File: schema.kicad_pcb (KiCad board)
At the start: 2 copper layers, 59.7 x 41.3 mm, 4 parts, among them U1 74HC595D, U2 74HC595D, U5 28C256

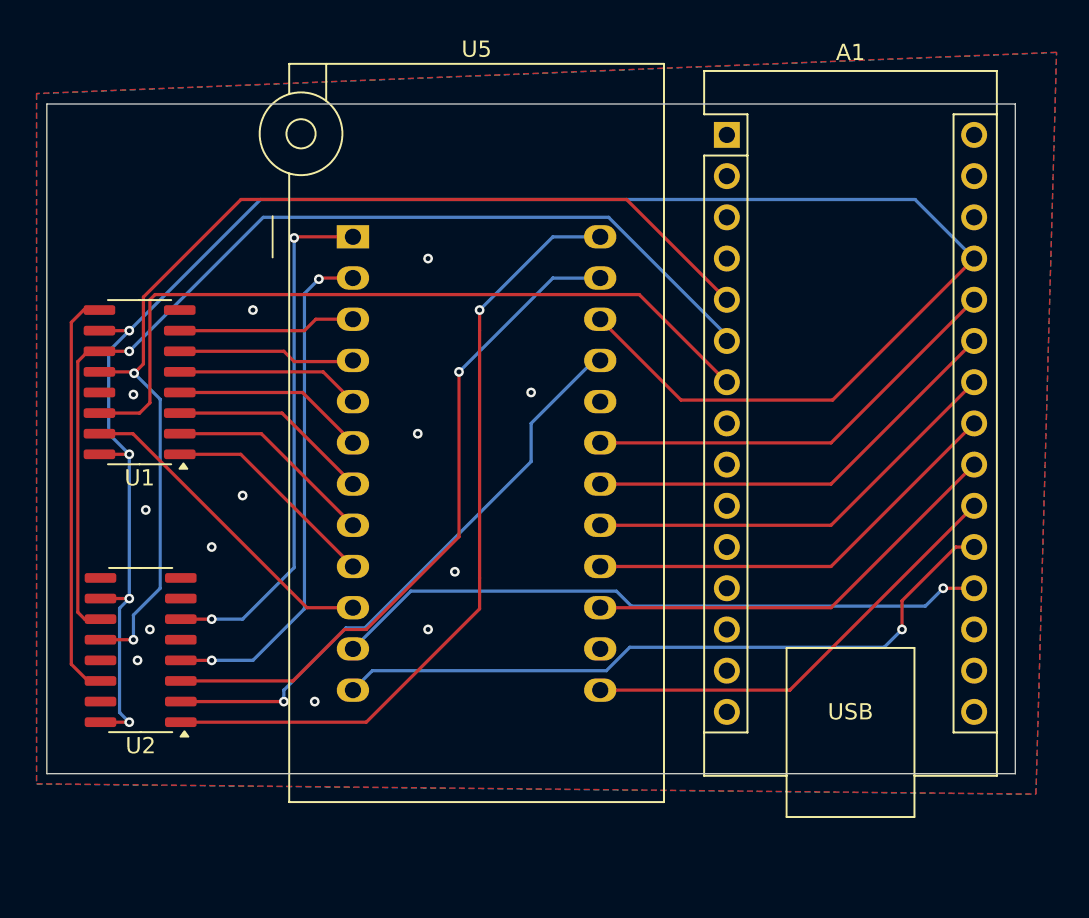
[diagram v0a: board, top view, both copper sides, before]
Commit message: fix-wrong-zif
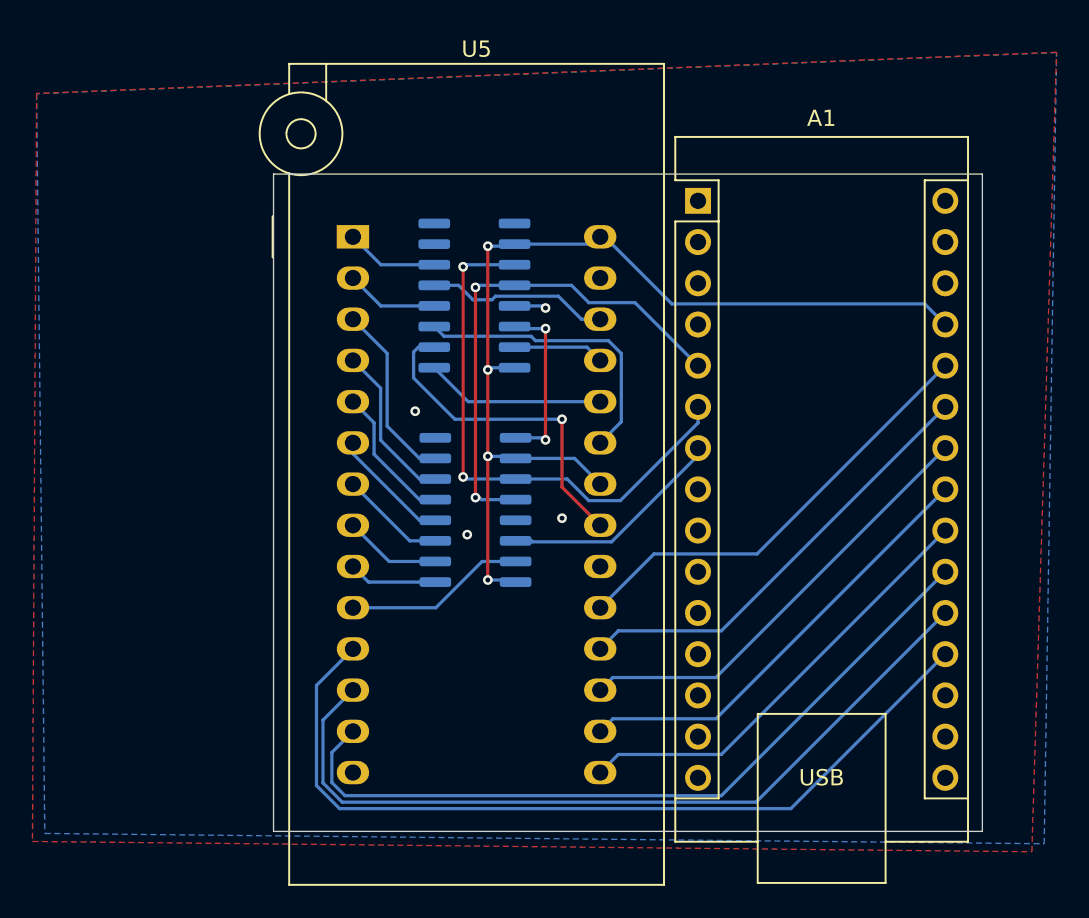
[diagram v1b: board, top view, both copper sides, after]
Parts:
- U1, U2: moved to B.Cu
- U5: value 28C256 -> AT28C256-15PU; footprint Socket:DIP_Socket-24_W11.9_W12.7_W15.24_W17.78_W18.5_3M_224-1275-00-0602J -> Socket:DIP_Socket-28_W11.9_W12.7_W15.24_W17.78_W18.5_3M_228-1277-00-0602J
- moved U2 30.0 mm to (133.0, 88.6), turned to 0 degrees
- moved U1 22.1 mm to (133.1, 101.9), turned to 0 degrees
- moved A1 4.44 mm to (146.8, 82.8)
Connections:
- A1 pad 27: /+5V -> +5VD
- U1 pad 10: /+5V -> +5VD
- U1 pad 16: /+5V -> +5VD
- U2 pad 10: /+5V -> +5VD
- U2 pad 16: /+5V -> +5VD
- U5 pad 22: /+5V -> +5VD
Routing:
- net /+5V: track 118.6 -> 0.00 mm, vias 4 -> 0
- net +5VD: track 0.00 -> 62.3 mm, vias 0 -> 4
- net Net-(U2-QB): track 49.0 -> 11.1 mm, vias 1 -> 0
- net Net-(A1-D2): track 67.9 -> 31.2 mm
- net Net-(A1-D4): track 47.7 -> 13.9 mm
- net Net-(A1-D3): track 64.1 -> 34.2 mm, vias 1 -> 2
- net Net-(U2-QG): track 32.3 -> 5.72 mm, vias 2 -> 0
- net Net-(U2-QE): track 31.8 -> 5.72 mm, vias 2 -> 0
- net Net-(U2-QD): track 42.1 -> 18.3 mm, vias 1 -> 0
- net Net-(A1-A2): track 27.8 -> 47.6 mm
- net Net-(U2-QC): track 36.4 -> 20.7 mm
- net Net-(U1-QH'): track 25.3 -> 10.7 mm, vias 0 -> 2
- net Net-(A1-A0): track 40.6 -> 52.6 mm, vias 1 -> 0
- net Net-(U2-QF): track 0.00 -> 11.3 mm
- net Net-(U1-QA): track 20.1 -> 11.2 mm
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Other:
- board size 59.7 x 41.3 mm -> 43.7 x 40.5 mm
- board text added: "Erinnerlichkeit V0.0.3 Proliecan"

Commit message: small corrections
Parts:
- added C1: 100nC, Capacitor_SMD:C_0805_2012Metric_Pad1.18x1.45mm_HandSolder, B.Cu at (143.3, 82.8)
- added C2: 100nC, Capacitor_SMD:C_0805_2012Metric_Pad1.18x1.45mm_HandSolder, B.Cu at (158.2, 90.7)
- added C3: 100nC, Capacitor_SMD:C_0805_2012Metric_Pad1.18x1.45mm_HandSolder, B.Cu at (132.8, 111.5)
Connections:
- net Net-(A1-A0) renamed /D0
- net Net-(A1-A1) renamed /D1
- net Net-(A1-A2) renamed /D2
- net Net-(A1-A3) renamed /D3
- net Net-(A1-A6) renamed /D6
- net Net-(A1-A7) renamed /D7
- net Net-(A1-SCL/A5) renamed /D5
- net Net-(A1-SDA/A4) renamed /D4
- net Net-(U1-QA) renamed /A0
- net Net-(U1-QB) renamed /A1
- net Net-(U1-QC) renamed /A2
- net Net-(U1-QD) renamed /A3
- net Net-(U1-QE) renamed /A4
- net Net-(U1-QF) renamed /A5
- net Net-(U1-QG) renamed /A6
- net Net-(U1-QH) renamed /A7
- net Net-(U2-QA) renamed /A8
- net Net-(U2-QB) renamed /A9
- net Net-(U2-QC) renamed /A10
- net Net-(U2-QD) renamed /A11
- net Net-(U2-QE) renamed /A12
- net Net-(U2-QF) renamed /A13
- net Net-(U2-QG) renamed /A14
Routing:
- net +5VD: track 62.3 -> 77.0 mm

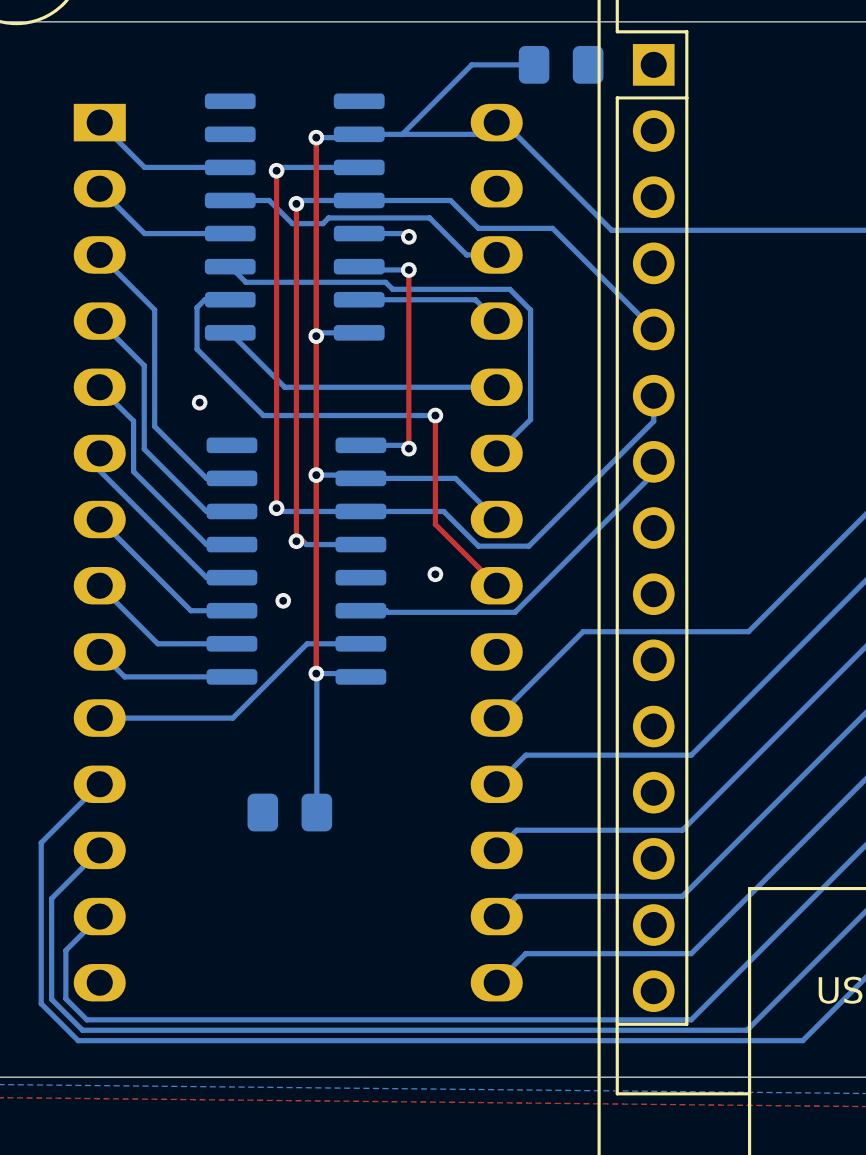
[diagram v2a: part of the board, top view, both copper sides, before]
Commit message: Route traces (with warnings)
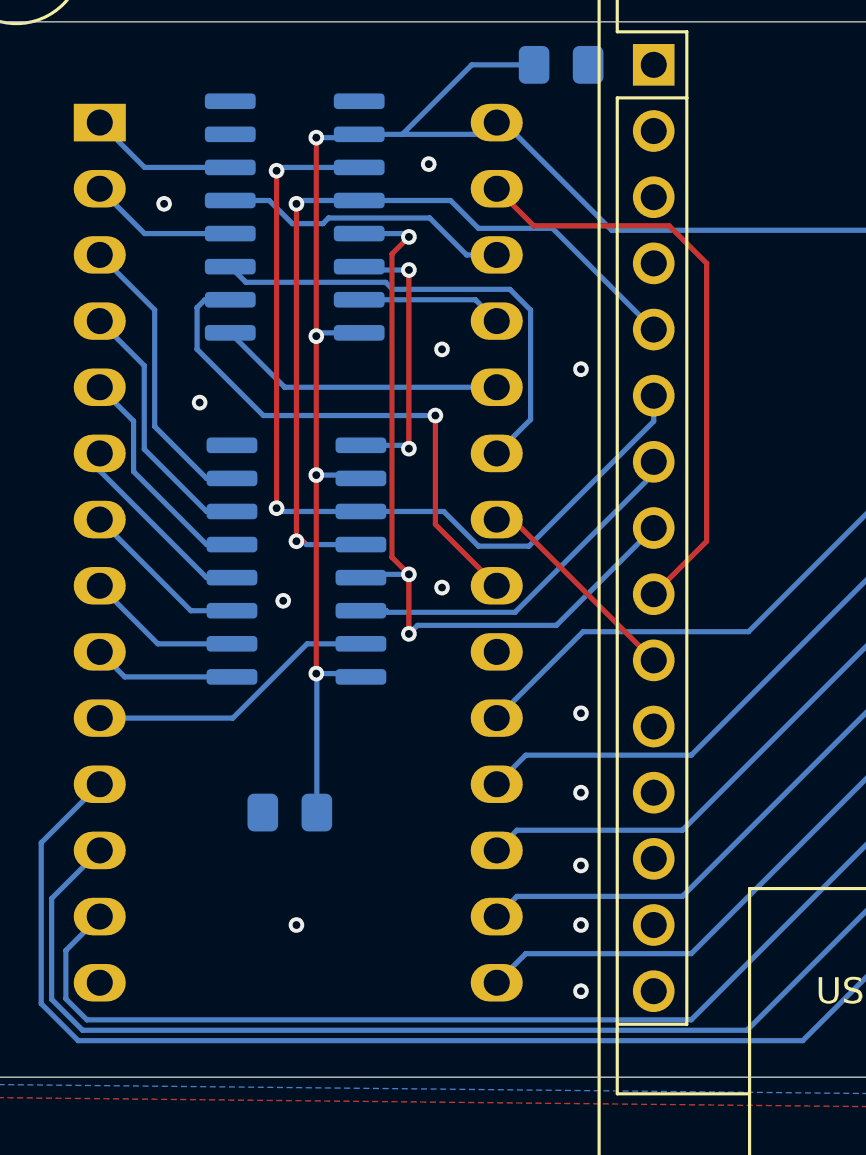
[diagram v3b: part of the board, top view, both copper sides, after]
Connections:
- A1 pad 10: unconnected-(A1-D7-Pad10) -> Net-(A1-D7)
- A1 pad 8: unconnected-(A1-D5-Pad8) -> Net-(A1-D5)
- A1 pad 9: unconnected-(A1-D6-Pad9) -> Net-(A1-D6)
- U1 pad 13: GNDD -> Net-(A1-D5)
- U2 pad 13: GNDD -> Net-(A1-D5)
- U5 pad 22: +5VD -> Net-(A1-D7)
- U5 pad 27: GNDD -> Net-(A1-D6)
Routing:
- net Net-(A1-D5): track 0.00 -> 30.7 mm, vias 0 -> 3
- net Net-(A1-D6): track 0.00 -> 22.8 mm
- net Net-(A1-D7): track 0.00 -> 8.27 mm
- net +5VD: track 77.0 -> 71.1 mm
- net GNDD: track 1.96 -> 0.00 mm, vias 4 -> 13
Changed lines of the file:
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@@
   (net 6 "Net-(A1-D3)")
   (net 7 "Net-(A1-D4)")
-  (net 8 "unconnected-(A1-D5-Pad8)")
-  (net 9 "unconnected-(A1-D6-Pad9)")
-  (net 10 "unconnected-(A1-D7-Pad10)")
+  (net 8 "Net-(A1-D5)")
+  (net 9 "Net-(A1-D6)")
+  (net 10 "Net-(A1-D7)")
   (net 11 "unconnected-(A1-D8-Pad11)")
   (net 12 "unconnected-(A1-D9-Pad12)")
@@
       (net 7 "Net-(A1-D4)") (pinfunction "D4") (pintype "bidirectional"))
     (pad "8" thru_hole oval (at 0 17.78) (size 1.6 1.6) (drill 1) (layers "*.Cu" "*.Mask")
-      (net 8 "unconnected-(A1-D5-Pad8)") (pinfunction "D5") (pintype "bidirectional"))
+      (net 8 "Net-(A1-D5)") (pinfunction "D5") (pintype "bidirectional"))
     (pad "9" thru_hole oval (at 0 20.32) (size 1.6 1.6) (drill 1) (layers "*.Cu" "*.Mask")
-      (net 9 "unconnected-(A1-D6-Pad9)") (pinfunction "D6") (pintype "bidirectional"))
+      (net 9 "Net-(A1-D6)") (pinfunction "D6") (pintype "bidirectional"))
     (pad "10" thru_hole oval (at 0 22.86) (size 1.6 1.6) (drill 1) (layers "*.Cu" "*.Mask")
-      (net 10 "unconnected-(A1-D7-Pad10)") (pinfunction "D7") (pintype "bidirectional"))
+      (net 10 "Net-(A1-D7)") (pinfunction "D7") (pintype "bidirectional"))
     (pad "11" thru_hole oval (at 0 25.4) (size 1.6 1.6) (drill 1) (layers "*.Cu" "*.Mask")
       (net 11 "unconnected-(A1-D8-Pad11)") (pinfunction "D8") (pintype "bidirectional"))
@@
       (net 39 "/A10") (pinfunction "A10") (pintype "input"))
     (pad "22" thru_hole oval (at 15.24 15.24) (size 2 1.44) (drill 1) (layers "*.Cu" "*.Mask")
-      (net 47 "+5VD") (pinfunction "~{OE}") (pintype "input"))
+      (net 10 "Net-(A1-D7)") (pinfunction "~{OE}") (pintype "input"))
     (pad "23" thru_hole oval (at 15.24 12.7) (size 2 1.44) (drill 1) (layers "*.Cu" "*.Mask")
       (net 40 "/A11") (pinfunction "A11") (pintype "input"))
@@
       (net 42 "/A13") (pinfunction "A13") (pintype "input"))
     (pad "27" thru_hole oval (at 15.24 2.54) (size 2 1.44) (drill 1) (layers "*.Cu" "*.Mask")
-      (net 4 "GNDD") (pinfunction "~{WE}") (pintype "input"))
+      (net 9 "Net-(A1-D6)") (pinfunction "~{WE}") (pintype "input"))
     (pad "28" thru_hole oval (at 15.24 0) (size 2 1.44) (drill 1) (layers "*.Cu" "*.Mask")
       (net 47 "+5VD") (pinfunction "VCC") (pintype "power_in"))
@@
       (net 5 "Net-(A1-D2)") (pinfunction "RCLK") (pintype "input"))
     (pad "13" smd roundrect (at 2.475 0.635) (size 1.95 0.6) (layers "B.Cu" "B.Paste" "B.Mask") (roundrect_rratio 0.25)
-      (net 4 "GNDD") (pinfunction "~{OE}") (pintype "input"))
+      (net 8 "Net-(A1-D5)") (pinfunction "~{OE}") (pintype "input"))
     (pad "14" smd roundrect (at 2.475 1.905) (size 1.95 0.6) (layers "B.Cu" "B.Paste" "B.Mask") (roundrect_rratio 0.25)
       (net 7 "Net-(A1-D4)") (pinfunction "SER") (pintype "input"))
@@
       (net 5 "Net-(A1-D2)") (pinfunction "RCLK") (pintype "input"))
     (pad "13" smd roundrect (at 2.475 0.635) (size 1.95 0.6) (layers "B.Cu" "B.Paste" "B.Mask") (roundrect_rratio 0.25)
-      (net 4 "GNDD") (pinfunction "~{OE}") (pintype "input"))
+      (net 8 "Net-(A1-D5)") (pinfunction "~{OE}") (pintype "input"))
     (pad "14" smd roundrect (at 2.475 1.905) (size 1.95 0.6) (layers "B.Cu" "B.Paste" "B.Mask") (roundrect_rratio 0.25)
       (net 36 "Net-(U1-QH')") (pinfunction "SER") (pintype "input"))
@@
     (effects (font (size 1.5 1.5) (thickness 0.3) bold) (justify left bottom mirror))
   )
-  (via (at 138.43 102.362) (size 0.6) (drill 0.3) (layers "F.Cu" "B.Cu") (free) (net 4))
+  (via (at 144.018 113.538) (size 0.6) (drill 0.3) (layers "F.Cu" "B.Cu") (free) (net 4))
+  (via (at 144.018 107.696) (size 0.6) (drill 0.3) (layers "F.Cu" "B.Cu") (free) (net 4))
+  (via (at 144.018 94.488) (size 0.6) (drill 0.3) (layers "F.Cu" "B.Cu") (free) (net 4))
+  (via (at 144.018 118.364) (size 0.6) (drill 0.3) (layers "F.Cu" "B.Cu") (free) (net 4))
+  (via (at 138.684 93.726) (size 0.6) (drill 0.3) (layers "F.Cu" "B.Cu") (free) (net 4))
   (via (at 132.588 103.378) (size 0.6) (drill 0.3) (layers "F.Cu" "B.Cu") (free) (net 4))
-  (via (at 137.414 89.408) (size 0.6) (drill 0.3) (layers "F.Cu" "B.Cu") (net 4))
+  (via (at 128.016 88.138) (size 0.6) (drill 0.3) (layers "F.Cu" "B.Cu") (free) (net 4))
+  (via (at 144.018 110.744) (size 0.6) (drill 0.3) (layers "F.Cu" "B.Cu") (free) (net 4))
+  (via (at 133.096 115.824) (size 0.6) (drill 0.3) (layers "F.Cu" "B.Cu") (free) (net 4))
+  (via (at 144.018 115.824) (size 0.6) (drill 0.3) (layers "F.Cu" "B.Cu") (free) (net 4))
+  (via (at 138.684 102.87) (size 0.6) (drill 0.3) (layers "F.Cu" "B.Cu") (free) (net 4))
+  (via (at 138.176 86.614) (size 0.6) (drill 0.3) (layers "F.Cu" "B.Cu") (free) (net 4))
   (via (at 129.380315 95.76949) (size 0.6) (drill 0.3) (layers "F.Cu" "B.Cu") (free) (net 4))
-  (segment (start 135.506 89.281) (end 137.287 89.281) (width 0.2) (layer "B.Cu") (net 4))
-  (segment (start 137.287 89.281) (end 137.414 89.408) (width 0.2) (layer "B.Cu") (net 4))
   (segment (start 133.096 100.838) (end 133.096 88.138) (width 0.2) (layer "F.Cu") (net 5))
   (segment (start 133.35 101.092) (end 133.096 100.838) (width 0.2) (layer "F.Cu") (net 5))
@@
   (segment (start 141.487498 103.82) (end 146.812 98.495498) (width 0.2) (layer "B.Cu") (net 7))
   (segment (start 136.545999 103.759) (end 136.606999 103.82) (width 0.2) (layer "B.Cu") (net 7))
+  (segment (start 136.764 101.712) (end 137.414 102.362) (width 0.2) (layer "F.Cu") (net 8))
+  (segment (start 137.414 89.408) (end 136.764 90.058) (width 0.2) (layer "F.Cu") (net 8))
+  (segment (start 137.414 102.362) (end 137.414 104.648) (width 0.2) (layer "F.Cu") (net 8))
+  (segment (start 136.764 90.058) (end 136.764 101.712) (width 0.2) (layer "F.Cu") (net 8))
+  (via (at 137.414 104.648) (size 0.6) (drill 0.3) (layers "F.Cu" "B.Cu") (net 8))
+  (via (at 137.414 89.408) (size 0.6) (drill 0.3) (layers "F.Cu" "B.Cu") (net 8))
+  (via (at 137.414 102.362) (size 0.6) (drill 0.3) (layers "F.Cu" "B.Cu") (net 8))
+  (segment (start 137.414 102.362) (end 135.698 102.362) (width 0.2) (layer "B.Cu") (net 8))
+  (segment (start 135.506 89.281) (end 137.287 89.281) (width 0.2) (layer "B.Cu") (net 8))
+  (segment (start 137.287 89.281) (end 137.414 89.408) (width 0.2) (layer "B.Cu") (net 8))
+  (segment (start 137.414 104.648) (end 137.742 104.32) (width 0.2) (layer "B.Cu") (net 8))
+  (segment (start 135.698 102.362) (end 135.571 102.489) (width 0.2) (layer "B.Cu") (net 8))
+  (segment (start 137.742 104.32) (end 143.076 104.32) (width 0.2) (layer "B.Cu") (net 8))
+  (segment (start 143.076 104.32) (end 146.812 100.584) (width 0.2) (layer "B.Cu") (net 8))
+  (segment (start 142.209 88.984) (end 147.404 88.984) (width 0.2) (layer "F.Cu") (net 9))
+  (segment (start 148.844 101.092) (end 146.812 103.124) (width 0.2) (layer "F.Cu") (net 9))
+  (segment (start 140.785 87.56) (end 142.209 88.984) (width 0.2) (layer "F.Cu") (net 9))
+  (segment (start 147.404 88.984) (end 148.844 90.424) (width 0.2) (layer "F.Cu") (net 9))
+  (segment (start 148.844 90.424) (end 148.844 101.092) (width 0.2) (layer "F.Cu") (net 9))
+  (segment (start 141.408 100.26) (end 146.812 105.664) (width 0.2) (layer "F.Cu") (net 10))
+  (segment (start 140.785 100.26) (end 141.408 100.26) (width 0.2) (layer "F.Cu") (net 10))
   (segment (start 152.532 120.264) (end 124.720628 120.264) (width 0.2) (layer "B.Cu") (net 19))
   (segment (start 123.298 118.841371) (end 123.298 112.667) (width 0.2) (layer "B.Cu") (net 19))
@@
   (segment (start 141.065 85.02) (end 145.199 89.154) (width 0.2) (layer "B.Cu") (net 47))
   (segment (start 145.199 89.154) (end 160.782 89.154) (width 0.2) (layer "B.Cu") (net 47))
-  (segment (start 135.571 98.679) (end 139.204 98.679) (width 0.2) (layer "B.Cu") (net 47))
   (segment (start 135.379 85.598) (end 135.506 85.471) (width 0.2) (layer "B.Cu") (net 47))
   (segment (start 133.858 98.552) (end 135.444 98.552) (width 0.2) (layer "B.Cu") (net 47))
@@
   (segment (start 137.16 85.471) (end 140.334 85.471) (width 0.2) (layer "B.Cu") (net 47))
   (segment (start 142.4725 82.804) (end 139.827 82.804) (width 0.2) (layer "B.Cu") (net 47))
-  (segment (start 139.204 98.679) (end 140.785 100.26) (width 0.2) (layer "B.Cu") (net 47))
   (segment (start 140.334 85.471) (end 140.785 85.02) (width 0.2) (layer "B.Cu") (net 47))
   (segment (start 161.798 90.678) (end 162.052 90.424) (width 0.2) (layer "B.Cu") (net 47))
